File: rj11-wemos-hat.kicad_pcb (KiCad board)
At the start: 2 copper layers, 2 parts

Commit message: First complete Draft
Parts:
- removed the G*** at (22.4, 182.3)
- added AN1: Conn_01x03, Connector_PinHeader_2.54mm:PinHeader_1x03_P2.54mm_Vertical, F.Cu at (68.2, 74.4)
- added H1: MountingHole, MountingHole:MountingHole_3mm, F.Cu at (100.0, 40.8)
- added J0: Conn_02x12_Odd_Even, Connector_PinSocket_2.54mm:PinSocket_2x12_P2.54mm_Vertical, B.Cu at (70.5, 68.7)
- added J1: RJ10, Connector_RJ:RJ12_Amphenol_54601, F.Cu at (76.7, 68.5)
- added J10: SDA, Connector_Wire:SolderWire-0.15sqmm_1x01_D0.5mm_OD1.5mm, F.Cu at (92.9, 51.0)
- added J11: D6, Connector_Wire:SolderWire-0.15sqmm_1x01_D0.5mm_OD1.5mm, F.Cu at (89.9, 51.0)
- added J12: D5, Connector_Wire:SolderWire-0.15sqmm_1x01_D0.5mm_OD1.5mm, F.Cu at (86.8, 51.0)
- added J13: D7, Connector_Wire:SolderWire-0.15sqmm_1x01_D0.5mm_OD1.5mm, F.Cu at (83.8, 51.0)
- added J14: D8, Connector_Wire:SolderWire-0.15sqmm_1x01_D0.5mm_OD1.5mm, F.Cu at (80.7, 51.0)
- added J15: D0, Connector_Wire:SolderWire-0.15sqmm_1x01_D0.5mm_OD1.5mm, F.Cu at (77.7, 51.0)
- added J16: D4, Connector_Wire:SolderWire-0.15sqmm_1x01_D0.5mm_OD1.5mm, F.Cu at (74.6, 51.0)
- added J2: RJ10, Connector_RJ:RJ12_Amphenol_54601, F.Cu at (91.3, 68.5)
- added J6: D3, Connector_Wire:SolderWire-0.15sqmm_1x01_D0.5mm_OD1.5mm, F.Cu at (99.0, 46.7)
- added J7: RX, Connector_Wire:SolderWire-0.15sqmm_1x01_D0.5mm_OD1.5mm, F.Cu at (102.1, 51.0)
- added J8: TX, Connector_Wire:SolderWire-0.15sqmm_1x01_D0.5mm_OD1.5mm, F.Cu at (99.0, 51.0)
- added J9: SCL, Connector_Wire:SolderWire-0.15sqmm_1x01_D0.5mm_OD1.5mm, F.Cu at (96.0, 51.0)
- added JP1: ~, Connector_PinHeader_2.54mm:PinHeader_1x02_P2.54mm_Vertical, F.Cu at (78.9, 58.1)
- added JP2: ~, Connector_PinHeader_2.54mm:PinHeader_1x02_P2.54mm_Vertical, F.Cu at (93.5, 58.1)
- added JR1: Conn_01x03, Connector_PinHeader_2.54mm:PinHeader_1x03_P2.54mm_Vertical, F.Cu at (74.7, 63.1)
- added R1: 10k, Resistor_SMD:R_0603_1608Metric_Pad0.98x0.95mm_HandSolder, F.Cu at (65.2, 44.8)
- added R2: 10k, Resistor_SMD:R_0603_1608Metric_Pad0.98x0.95mm_HandSolder, F.Cu at (73.2, 44.8)
- added SW1: SW_Push, Button_Switch_THT:SW_PUSH_6mm, F.Cu at (75.7, 40.4)
- added SW2: SW_Push, Button_Switch_THT:SW_PUSH_6mm, F.Cu at (87.3, 40.4)
- added locked: Conn_01x03, Connector_PinHeader_2.54mm:PinHeader_1x03_P2.54mm_Vertical, F.Cu at (89.3, 63.1)
- moved G*** 134.4 mm to (84.3, 61.7)
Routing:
- net GND: track 0.00 -> 94.5 mm, vias 0 -> 3
- net +3.3V: track 0.00 -> 89.7 mm
- net D0_GPIO16: track 0.00 -> 53.2 mm, vias 0 -> 1
- net D3_GPIO0: track 0.00 -> 53.1 mm
- net RX: track 0.00 -> 39.8 mm
- net +5V: track 0.00 -> 37.5 mm
- net D1_SCL: track 0.00 -> 36.9 mm
- net TX: track 0.00 -> 34.3 mm
- net D2_SDA: track 0.00 -> 32.0 mm
- net A0_ANL: track 0.00 -> 31.8 mm
- net ~{RESET}: track 0.00 -> 27.6 mm
- net D6_MISO: track 0.00 -> 23.3 mm
- net D5_SCK: track 0.00 -> 20.3 mm
- net D7_MOSI: track 0.00 -> 20.0 mm
- net D8_CS: track 0.00 -> 17.3 mm
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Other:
- board outline added: 39.3 x 46.5 mm

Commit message: Initial version (Revision 1.0)
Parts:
- J10, J11, J12, J13, J14, J15, J16, J6, J7, J8, J9: footprint Connector_Wire:SolderWire-0.15sqmm_1x01_D0.5mm_OD1.5mm -> Chof747 Footprints:Solder Pad 1x1 1.5x3
- JP1, JP2: footprint Connector_PinHeader_2.54mm:PinHeader_1x02_P2.54mm_Vertical -> Chof747 Footprints:Solder Pad 1x2 1.5x3
- SW1: value SW_Push -> RST
- SW2: value SW_Push -> Flash
- moved J1 1.71 mm to (76.7, 70.2)
- moved J2 1.71 mm to (91.3, 70.2)
- moved J6 1.23 mm to (99.6, 45.6), turned to 90 degrees
- turned J12 to 0 degrees
- turned JP1 to 0 degrees
- turned JP2 to 0 degrees
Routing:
- net Net-(JP2-Pin_2): track 11.3 -> 17.5 mm, vias 0 -> 1
- net TX: track 34.3 -> 38.6 mm, vias 0 -> 1
- net GND: track 94.5 -> 91.7 mm, vias 3 -> 1
- net Net-(JP1-Pin_2): track 11.3 -> 13.6 mm, vias 0 -> 1
- net RX: track 39.8 -> 42.0 mm
- net D8_CS: track 17.3 -> 15.2 mm
- net D5_SCK: track 20.3 -> 22.2 mm
- net Net-(JP2-Pin_1): track 13.3 -> 15.2 mm, vias 0 -> 1
- net Net-(JP1-Pin_1): track 13.3 -> 15.1 mm, vias 0 -> 1
- net /PWR_2: track 8.72 -> 10.5 mm
- net /PWR_1: track 8.72 -> 10.5 mm
- net D3_GPIO0: track 53.1 -> 52.0 mm
- net D0_GPIO16: track 53.2 -> 53.3 mm, vias 1 -> 2
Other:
- outline, holes or cut-outs redrawn

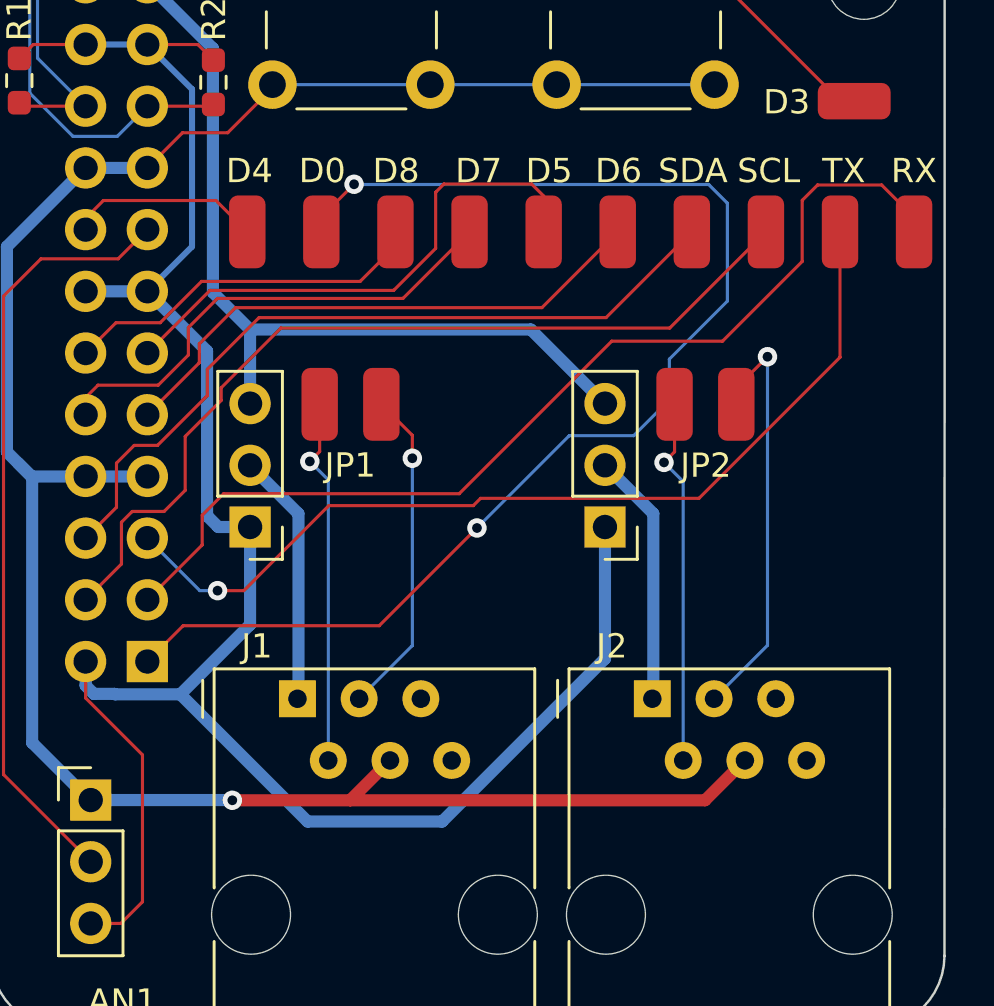
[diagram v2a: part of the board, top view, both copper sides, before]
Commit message: corrected RJ12 socket Connector
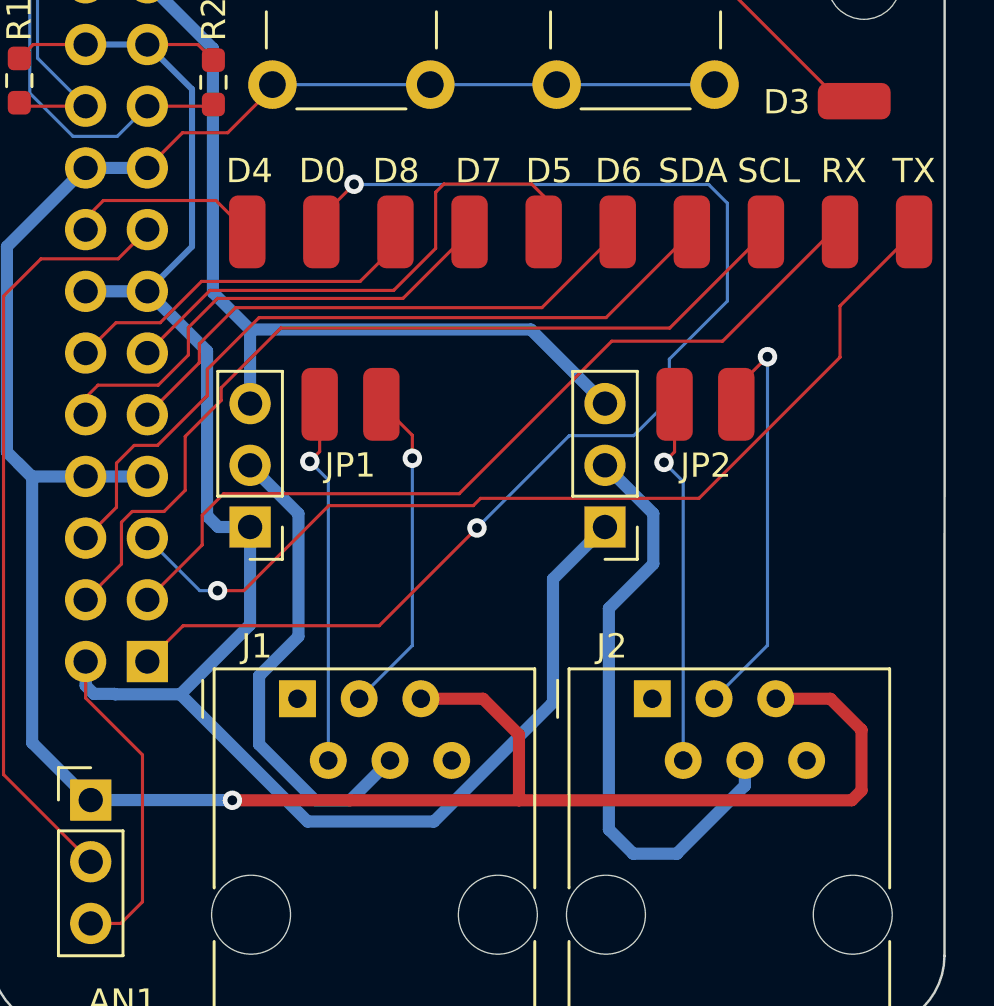
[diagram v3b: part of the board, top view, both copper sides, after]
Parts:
- J7: value RX -> TX
- J8: value TX -> RX
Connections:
- J1 pad 1: /PWR_1 -> (no net)
- J1 pad 4: GND -> /PWR_1
- J1 pad 5: (no net) -> GND
- J2 pad 1: /PWR_2 -> (no net)
- J2 pad 4: GND -> /PWR_2
- J2 pad 5: (no net) -> GND
- J7 pad 1: RX -> TX
- J8 pad 1: TX -> RX
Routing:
- net GND: track 91.7 -> 107.6 mm
- net /PWR_2: track 10.5 -> 24.8 mm
- net /PWR_1: track 10.5 -> 20.0 mm
- net RX: track 42.0 -> 35.5 mm
- net TX: track 38.6 -> 39.8 mm
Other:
- board text added: "RJ12-Hat for WeMos MainsBoard"
- board text added: "v1.1 (2023)"

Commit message: Format changes and first assembly
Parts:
- moved J6 33.8 mm to (90.0, 78.0)
- moved AN1 33.8 mm to (58.5, 106.8)
- moved H1 33.8 mm to (90.4, 73.2)
- moved J0 33.8 mm to (60.9, 101.1)
- moved J1 33.8 mm to (67.0, 102.6)
- moved J10 33.8 mm to (83.3, 83.4)
- moved J11 33.8 mm to (80.2, 83.4)
- moved J12 33.8 mm to (77.2, 83.4)
- moved J13 33.8 mm to (74.1, 83.4)
- moved J14 33.8 mm to (71.1, 83.4)
- moved J15 33.8 mm to (68.0, 83.4)
- moved J16 33.8 mm to (65.0, 83.4)
- moved J2 33.8 mm to (81.7, 102.6)
- moved J7 33.8 mm to (92.4, 83.4)
- moved J8 33.8 mm to (89.4, 83.4)
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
